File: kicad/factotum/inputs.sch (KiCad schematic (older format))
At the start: 33 parts, among them J4 Conn_01x10_Female, J5 VOCT, J6 Conn_01x10_Male, J7 SCL, J8 CLK, SW1 MODE_SW, U4 MCP6004, U5 ADC128S022

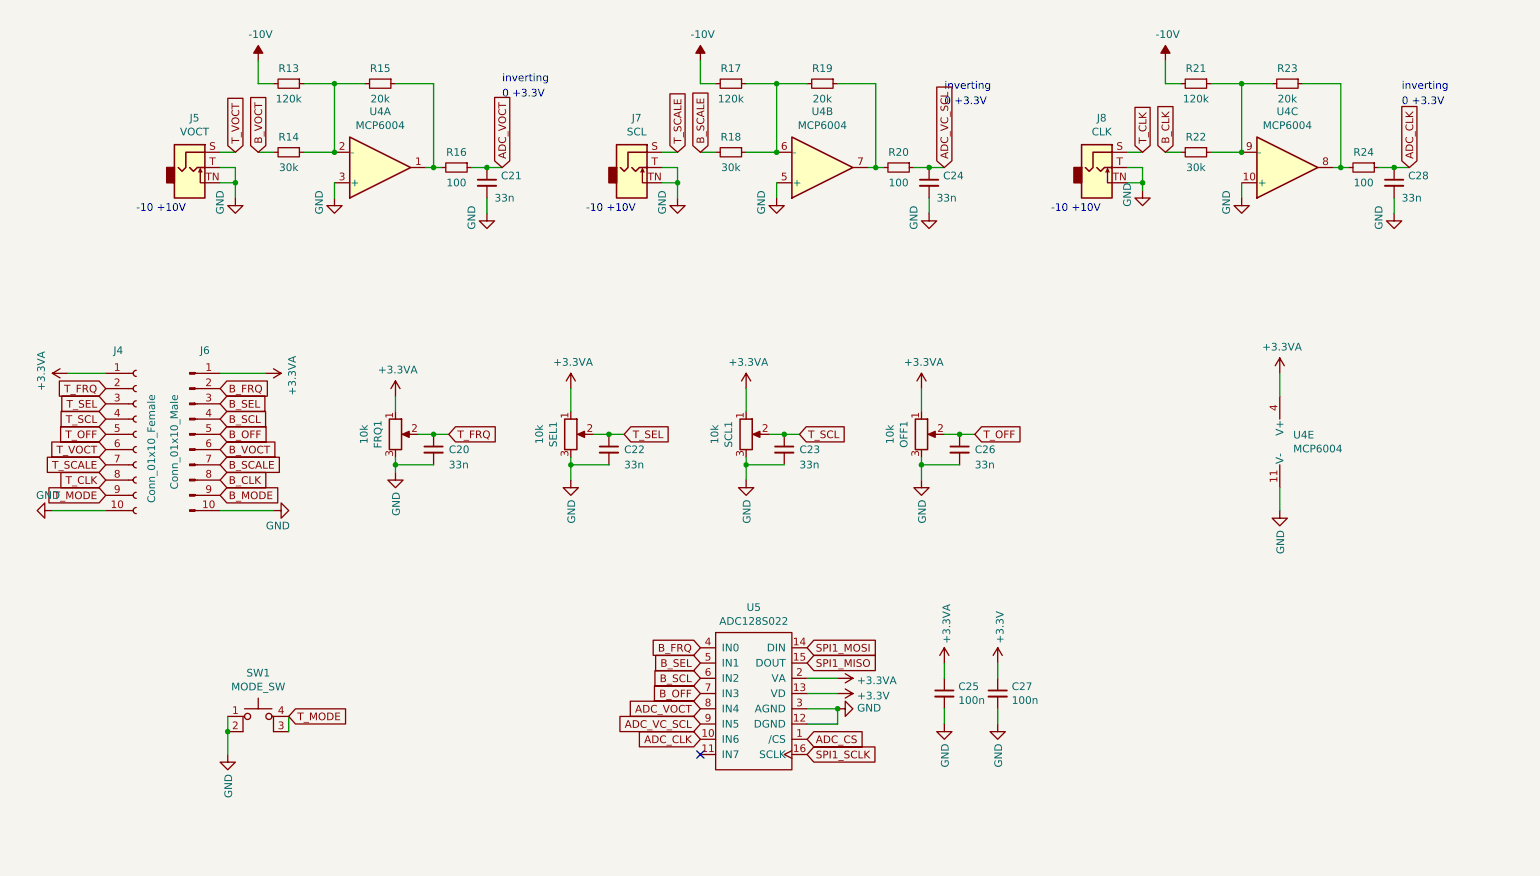
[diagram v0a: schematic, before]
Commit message: inital board layout done but not routed
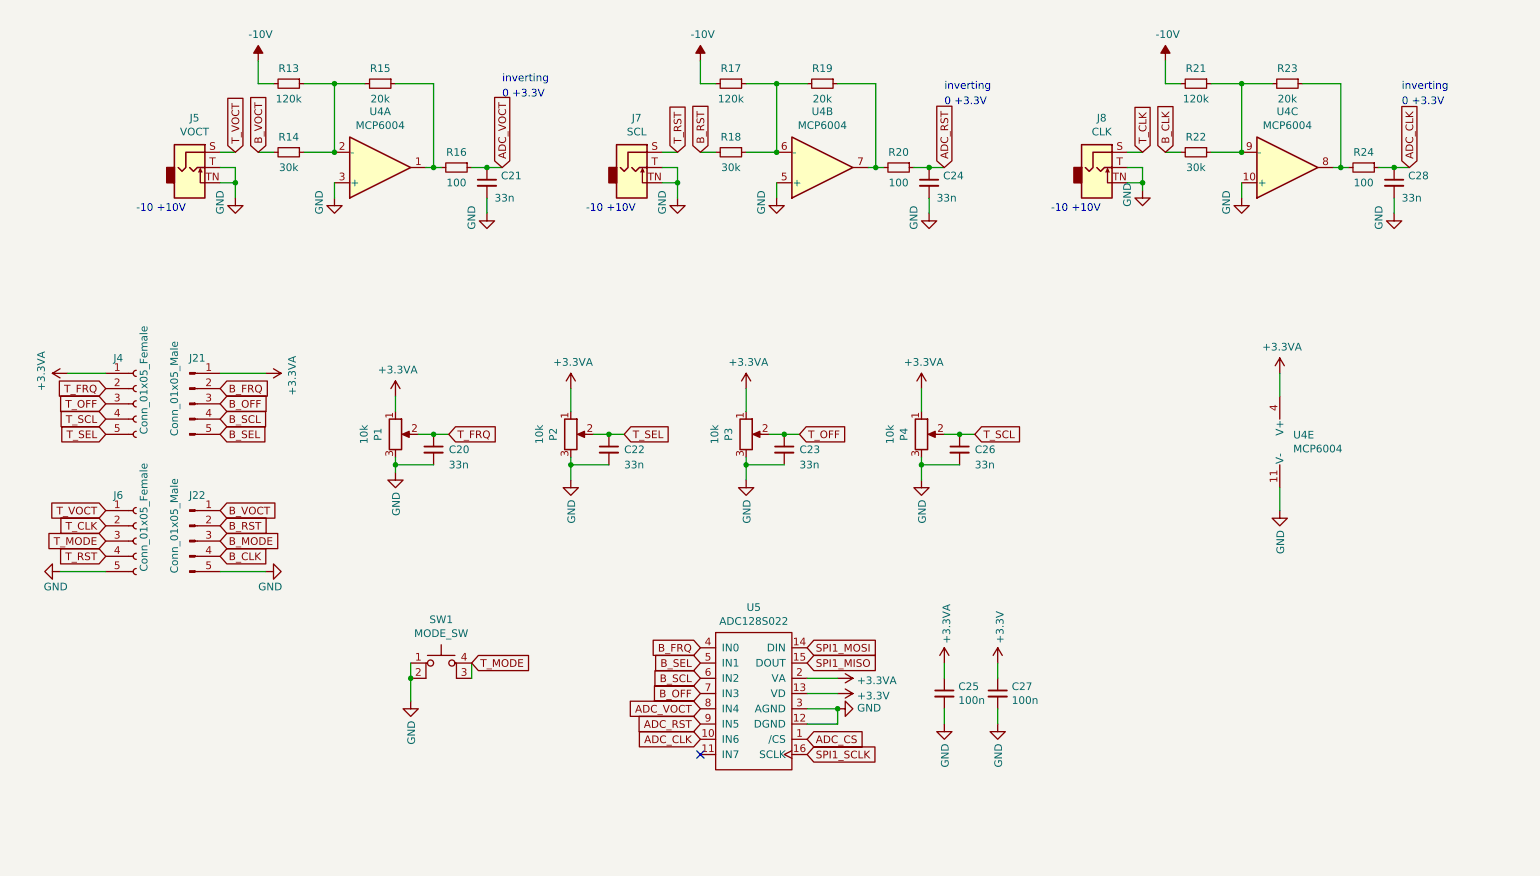
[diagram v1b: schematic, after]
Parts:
- removed J4: Conn_01x10_Female, Connector_PinSocket_1.27mm:PinSocket_1x10_P1.27mm_Vertical, symbol Connector:Conn_01x10_Female
- removed J6: Conn_01x10_Male, Connector_PinHeader_1.27mm:PinHeader_1x10_P1.27mm_Vertical, symbol Connector:Conn_01x10_Male
- added J21, J22: Conn_01x05_Male, Connector_PinHeader_2.54mm:PinHeader_1x05_P2.54mm_Vertical, symbol Connector:Conn_01x05_Male
- added J4, J6: Conn_01x05_Female, Connector_PinSocket_2.54mm:PinSocket_1x05_P2.54mm_Vertical, symbol Connector:Conn_01x05_Female
- J5: footprint (none) -> Connector_Audio:Jack_3.5mm_QingPu_WQP-PJ398SM_Vertical_CircularHoles
- renumbered FRQ1 to P1, SEL1 to P2, SCL1 to P3, OFF1 to P4
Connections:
- net +3.3VA: now also J21.1 (Pin_1), J4.1 (Pin_1)
- net B_CLK: now also J22.4 (Pin_4)
- net B_FRQ: now also J21.2 (Pin_2)
- net B_MODE: now also J22.3 (Pin_3)
- net B_OFF: now also J21.3 (Pin_3)
- net B_SCL: now also J21.4 (Pin_4)
- net B_SEL: now also J21.5 (Pin_5)
- net B_VOCT: now also J22.1 (Pin_1)
- net GND: now also J22.5 (Pin_5), J6.5 (Pin_5)
- net T_CLK: now also J6.2 (Pin_2)
- net T_FRQ: now also J4.2 (Pin_2)
- net T_MODE: now also J6.3 (Pin_3)
- net T_OFF: now also C23.1, P3.2, J4.3 (Pin_3); no longer C26.1, P4.2
- net T_SCL: now also C26.1, P4.2, J4.4 (Pin_4); no longer C23.1, P3.2
- net T_SEL: now also J4.5 (Pin_5)
- net T_VOCT: now also J6.1 (Pin_1)
- net ADC_VC_SCL renamed ADC_RST
- net B_SCALE renamed B_RST
- net B_RST: now also J22.2 (Pin_2)
- net T_SCALE renamed T_RST
- net T_RST: now also J6.4 (Pin_4)
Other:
- moved on the sheet: SW1
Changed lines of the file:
@@
 $EndComp
 Text GLabel 6600 1650 1    50   Input ~ 0
-ADC_VC_SCL
+ADC_RST
 Wire Wire Line
 	5300 1100 5500 1100
@@
 F 0 "J5" H 1682 1975 50  0000 C CNN
 F 1 "VOCT" H 1682 1884 50  0000 C CNN
-F 2 "" H 1650 1650 50  0001 C CNN
+F 2 "Connector_Audio:Jack_3.5mm_QingPu_WQP-PJ398SM_Vertical_CircularHoles" H 1650 1650 50  0001 C CNN
 F 3 "~" H 1650 1650 50  0001 C CNN
 	1    1650 1650
@@
 P 3000 3400
 AR Path="/60807EF6" Ref="FRQ?"  Part="1"
-AR Path="/606FF2F2/60807EF6" Ref="FRQ1"  Part="1"
-F 0 "FRQ1" V 2885 3400 50  0000 C CNN
+AR Path="/606FF2F2/60807EF6" Ref="P1"  Part="1"
+F 0 "P1" V 2885 3400 50  0000 C CNN
 F 1 "10k" V 2794 3400 50  0000 C CNN
 F 2 "Potentiometer_THT:Potentiometer_Alpha_RD901F-40-00D_Single_Vertical_CircularHoles" H 3000 3400 50  0001 C CNN
@@
 P 4150 3400
 AR Path="/6082088B" Ref="FRQ?"  Part="1"
-AR Path="/606FF2F2/6082088B" Ref="SEL1"  Part="1"
-F 0 "SEL1" V 4035 3400 50  0000 C CNN
+AR Path="/606FF2F2/6082088B" Ref="P2"  Part="1"
+F 0 "P2" V 4035 3400 50  0000 C CNN
 F 1 "10k" V 3944 3400 50  0000 C CNN
 F 2 "Potentiometer_THT:Potentiometer_Alpha_RD901F-40-00D_Single_Vertical_CircularHoles" H 4150 3400 50  0001 C CNN
@@
 Wire Wire Line
 	4150 3600 4150 3700
-Text GLabel 1850 3200 2    50   Input ~ 0
+Text GLabel 1850 3400 2    50   Input ~ 0
 B_SEL
 $Comp
@@
 P 5300 3400
 AR Path="/6082982D" Ref="FRQ?"  Part="1"
-AR Path="/606FF2F2/6082982D" Ref="SCL1"  Part="1"
-F 0 "SCL1" V 5185 3400 50  0000 C CNN
+AR Path="/606FF2F2/6082982D" Ref="P3"  Part="1"
+F 0 "P3" V 5185 3400 50  0000 C CNN
 F 1 "10k" V 5094 3400 50  0000 C CNN
 F 2 "Potentiometer_THT:Potentiometer_Alpha_RD901F-40-00D_Single_Vertical_CircularHoles" H 5300 3400 50  0001 C CNN
@@
 P 6450 3400
 AR Path="/60829C62" Ref="FRQ?"  Part="1"
-AR Path="/606FF2F2/60829C62" Ref="OFF1"  Part="1"
-F 0 "OFF1" V 6335 3400 50  0000 C CNN
+AR Path="/606FF2F2/60829C62" Ref="P4"  Part="1"
+F 0 "P4" V 6335 3400 50  0000 C CNN
 F 1 "10k" V 6244 3400 50  0000 C CNN
 F 2 "Potentiometer_THT:Potentiometer_Alpha_RD901F-40-00D_Single_Vertical_CircularHoles" H 6450 3400 50  0001 C CNN
@@
 Wire Wire Line
 	6450 3600 6450 3700
-Text GLabel 1850 3400 2    50   Input ~ 0
+Text GLabel 1850 3200 2    50   Input ~ 0
 B_OFF
 Text GLabel 5000 4800 0    50   Input ~ 0
@@
 ADC_VOCT
 Text GLabel 5000 5300 0    50   Input ~ 0
-ADC_VC_SCL
+ADC_RST
 Text GLabel 5000 5400 0    50   Input ~ 0
 ADC_CLK
@@
 L Switch:SW_MEC_5E SW1
 U 1 1 60C7CA31
-P 2100 5350
-F 0 "SW1" H 2100 5735 50  0000 C CNN
-F 1 "MODE_SW" H 2100 5644 50  0000 C CNN
-F 2 "Button_Switch_THT:SW_TH_Tactile_Omron_B3F-10xx" H 2100 5650 50  0001 C CNN
-F 3 "http://www.apem.com/int/index.php?controller=attachment&id_attachment=1371" H 2100 5650 50  0001 C CNN
-	1    2100 5350
+P 3300 5000
+F 0 "SW1" H 3300 5385 50  0000 C CNN
+F 1 "MODE_SW" H 3300 5294 50  0000 C CNN
+F 2 "Button_Switch_THT:SW_TH_Tactile_Omron_B3F-10xx" H 3300 5300 50  0001 C CNN
+F 3 "http://www.apem.com/int/index.php?controller=attachment&id_attachment=1371" H 3300 5300 50  0001 C CNN
+	1    3300 5000
 	1    0    0    -1
 $EndComp
@@
 L power:GND #PWR?
 U 1 1 60C7DEEC
-P 1900 5500
+P 3100 5150
 AR Path="/60C7DEEC" Ref="#PWR?"  Part="1"
 AR Path="/606FF2F2/60C7DEEC" Ref="#PWR031"  Part="1"
-F 0 "#PWR031" H 1900 5250 50  0001 C CNN
-F 1 "GND" V 1905 5372 50  0000 R CNN
-F 2 "" H 1900 5500 50  0001 C CNN
-F 3 "" H 1900 5500 50  0001 C CNN
-	1    1900 5500
-	1    0    0    -1
-$EndComp
-Wire Wire Line
-	1900 5500 1900 5350
-Connection ~ 1900 5350
-Wire Wire Line
-	1900 5350 1900 5250
-Text GLabel 2300 5250 2    50   Input ~ 0
+F 0 "#PWR031" H 3100 4900 50  0001 C CNN
+F 1 "GND" V 3105 5022 50  0000 R CNN
+F 2 "" H 3100 5150 50  0001 C CNN
+F 3 "" H 3100 5150 50  0001 C CNN
+	1    3100 5150
+	1    0    0    -1
+$EndComp
+Wire Wire Line
+	3100 5150 3100 5000
+Connection ~ 3100 5000
+Wire Wire Line
+	3100 5000 3100 4900
+Text GLabel 3500 4900 2    50   Input ~ 0
 T_MODE
 Wire Wire Line
-	2300 5250 2300 5350
-$Comp
-L Connector:Conn_01x10_Female J4
-U 1 1 5FC3B5C0
-P 1300 3400
-F 0 "J4" H 1150 3950 50  0000 L CNN
-F 1 "Conn_01x10_Female" V 1400 2950 50  0000 L CNN
-F 2 "Connector_PinSocket_1.27mm:PinSocket_1x10_P1.27mm_Vertical" H 1300 3400 50  0001 C CNN
-F 3 "~" H 1300 3400 50  0001 C CNN
-	1    1300 3400
-	1    0    0    -1
-$EndComp
-$Comp
-L Connector:Conn_01x10_Male J6
-U 1 1 5FC3DD64
-P 1650 3400
-F 0 "J6" H 1750 3950 50  0000 C CNN
-F 1 "Conn_01x10_Male" V 1550 3350 50  0000 C CNN
-F 2 "Connector_PinHeader_1.27mm:PinHeader_1x10_P1.27mm_Vertical" H 1650 3400 50  0001 C CNN
-F 3 "~" H 1650 3400 50  0001 C CNN
-	1    1650 3400
-	1    0    0    -1
-$EndComp
+	3500 4900 3500 5000
 Wire Wire Line
 	3000 3550 3000 3600
@@
 Text GLabel 4500 3400 2    50   Input ~ 0
 T_SEL
-Text GLabel 1100 3200 0    50   Input ~ 0
+Text GLabel 1100 3400 0    50   Input ~ 0
 T_SEL
 Connection ~ 5550 3400
@@
 Wire Wire Line
 	6700 3600 6450 3600
+Text GLabel 6800 3400 2    50   Input ~ 0
+T_SCL
 Text GLabel 5650 3400 2    50   Input ~ 0
-T_SCL
-Text GLabel 6800 3400 2    50   Input ~ 0
 T_OFF
-Text GLabel 1100 3400 0    50   Input ~ 0
+Text GLabel 1100 3200 0    50   Input ~ 0
 T_OFF
 Text GLabel 1100 3300 0    50   Input ~ 0
@@
 Text GLabel 1950 1550 1    50   Input ~ 0
 T_VOCT
-Text GLabel 1100 3500 0    50   Input ~ 0
+Text GLabel 1100 3900 0    50   Input ~ 0
 T_VOCT
 Text GLabel 2100 1550 1    50   Input ~ 0
 B_VOCT
-Text GLabel 1850 3500 2    50   Input ~ 0
+Text GLabel 1850 3900 2    50   Input ~ 0
 B_VOCT
 Text GLabel 4850 1550 1    50   Input ~ 0
-T_SCALE
+T_RST
 Wire Wire Line
 	8350 1550 8550 1550
 Connection ~ 8550 1550
 Text GLabel 5000 1550 1    50   Input ~ 0
-B_SCALE
+B_RST
 Text GLabel 7900 1550 1    50   Input ~ 0
 T_CLK
 Text GLabel 8050 1550 1    50   Input ~ 0
 B_CLK
-Text GLabel 1100 3600 0    50   Input ~ 0
-T_SCALE
-Text GLabel 1850 3600 2    50   Input ~ 0
-B_SCALE
-Text GLabel 1100 3700 0    50   Input ~ 0
+Text GLabel 1100 4200 0    50   Input ~ 0
+T_RST
+Text GLabel 1850 4000 2    50   Input ~ 0
+B_RST
+Text GLabel 1100 4000 0    50   Input ~ 0
 T_CLK
-Text GLabel 1850 3700 2    50   Input ~ 0
+Text GLabel 1850 4200 2    50   Input ~ 0
 B_CLK
-Text GLabel 1850 3800 2    50   Input ~ 0
+Text GLabel 1850 4100 2    50   Input ~ 0
 B_MODE
-Text GLabel 1100 3800 0    50   Input ~ 0
+Text GLabel 1100 4100 0    50   Input ~ 0
 T_MODE
 $Comp
@@
 L power:GND #PWR?
 U 1 1 5FE18FBB
-P 750 3900
+P 800 4300
 AR Path="/5FE18FBB" Ref="#PWR?"  Part="1"
 AR Path="/606FF2F2/5FE18FBB" Ref="#PWR029"  Part="1"
-F 0 "#PWR029" H 750 3650 50  0001 C CNN
-F 1 "GND" V 650 3950 50  0000 R CNN
-F 2 "" H 750 3900 50  0001 C CNN
-F 3 "" H 750 3900 50  0001 C CNN
-	1    750  3900
+F 0 "#PWR029" H 800 4050 50  0001 C CNN
+F 1 "GND" V 900 4350 50  0000 R CNN
+F 2 "" H 800 4300 50  0001 C CNN
+F 3 "" H 800 4300 50  0001 C CNN
+	1    800  4300
 	0    1    1    0
 $EndComp
@@
 L power:GND #PWR?
 U 1 1 5FE1CBFF
-P 2200 3900
+P 2150 4300
 AR Path="/5FE1CBFF" Ref="#PWR?"  Part="1"
 AR Path="/606FF2F2/5FE1CBFF" Ref="#PWR035"  Part="1"
-F 0 "#PWR035" H 2200 3650 50  0001 C CNN
-F 1 "GND" V 2100 3950 50  0000 R CNN
-F 2 "" H 2200 3900 50  0001 C CNN
-F 3 "" H 2200 3900 50  0001 C CNN
-	1    2200 3900
+F 0 "#PWR035" H 2150 4050 50  0001 C CNN
+F 1 "GND" V 2050 4350 50  0000 R CNN
+F 2 "" H 2150 4300 50  0001 C CNN
+F 3 "" H 2150 4300 50  0001 C CNN
+	1    2150 4300
 	0    -1   -1   0
 $EndComp
@@
 Wire Wire Line
 	1850 3000 2150 3000
-Wire Wire Line
-	750  3900 1100 3900
-Wire Wire Line
-	1850 3900 2200 3900
 Wire Wire Line
 	1850 1650 1950 1650
@@
 Wire Wire Line
 	9550 1850 9550 1950
+$Comp
+L Connector:Conn_01x05_Female J4
+U 1 1 5FD0067F
+P 1300 3200
+F 0 "J4" H 1150 3500 50  0000 L CNN
+F 1 "Conn_01x05_Female" V 1350 3000 50  0000 L CNN
+F 2 "Connector_PinSocket_2.54mm:PinSocket_1x05_P2.54mm_Vertical" H 1300 3200 50  0001 C CNN
+F 3 "~" H 1300 3200 50  0001 C CNN
+	1    1300 3200
+	1    0    0    -1
+$EndComp
+$Comp
+L Connector:Conn_01x05_Male J21
+U 1 1 5FD01CE2
+P 1650 3200
+F 0 "J21" H 1700 3500 50  0000 C CNN
+F 1 "Conn_01x05_Male" V 1550 3300 50  0000 C CNN
+F 2 "Connector_PinHeader_2.54mm:PinHeader_1x05_P2.54mm_Vertical" H 1650 3200 50  0001 C CNN
+F 3 "~" H 1650 3200 50  0001 C CNN
+	1    1650 3200
+	1    0    0    -1
+$EndComp
+$Comp
+L Connector:Conn_01x05_Female J6
+U 1 1 5FD0B497
+P 1300 4100
+F 0 "J6" H 1150 4400 50  0000 L CNN
+F 1 "Conn_01x05_Female" V 1350 3900 50  0000 L CNN
+F 2 "Connector_PinSocket_2.54mm:PinSocket_1x05_P2.54mm_Vertical" H 1300 4100 50  0001 C CNN
+F 3 "~" H 1300 4100 50  0001 C CNN
+	1    1300 4100
+	1    0    0    -1
+$EndComp
+$Comp
+L Connector:Conn_01x05_Male J22
+U 1 1 5FD0B85D
+P 1650 4100
+F 0 "J22" H 1700 4400 50  0000 C CNN
+F 1 "Conn_01x05_Male" V 1550 4200 50  0000 C CNN
+F 2 "Connector_PinHeader_2.54mm:PinHeader_1x05_P2.54mm_Vertical" H 1650 4100 50  0001 C CNN
+F 3 "~" H 1650 4100 50  0001 C CNN
+	1    1650 4100
+	1    0    0    -1
+$EndComp
+Wire Wire Line
+	2150 4300 1850 4300
+Wire Wire Line
+	1100 4300 800  4300
 $EndSCHEMATC

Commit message: adding switches to inputs; fixing resistor components to 603
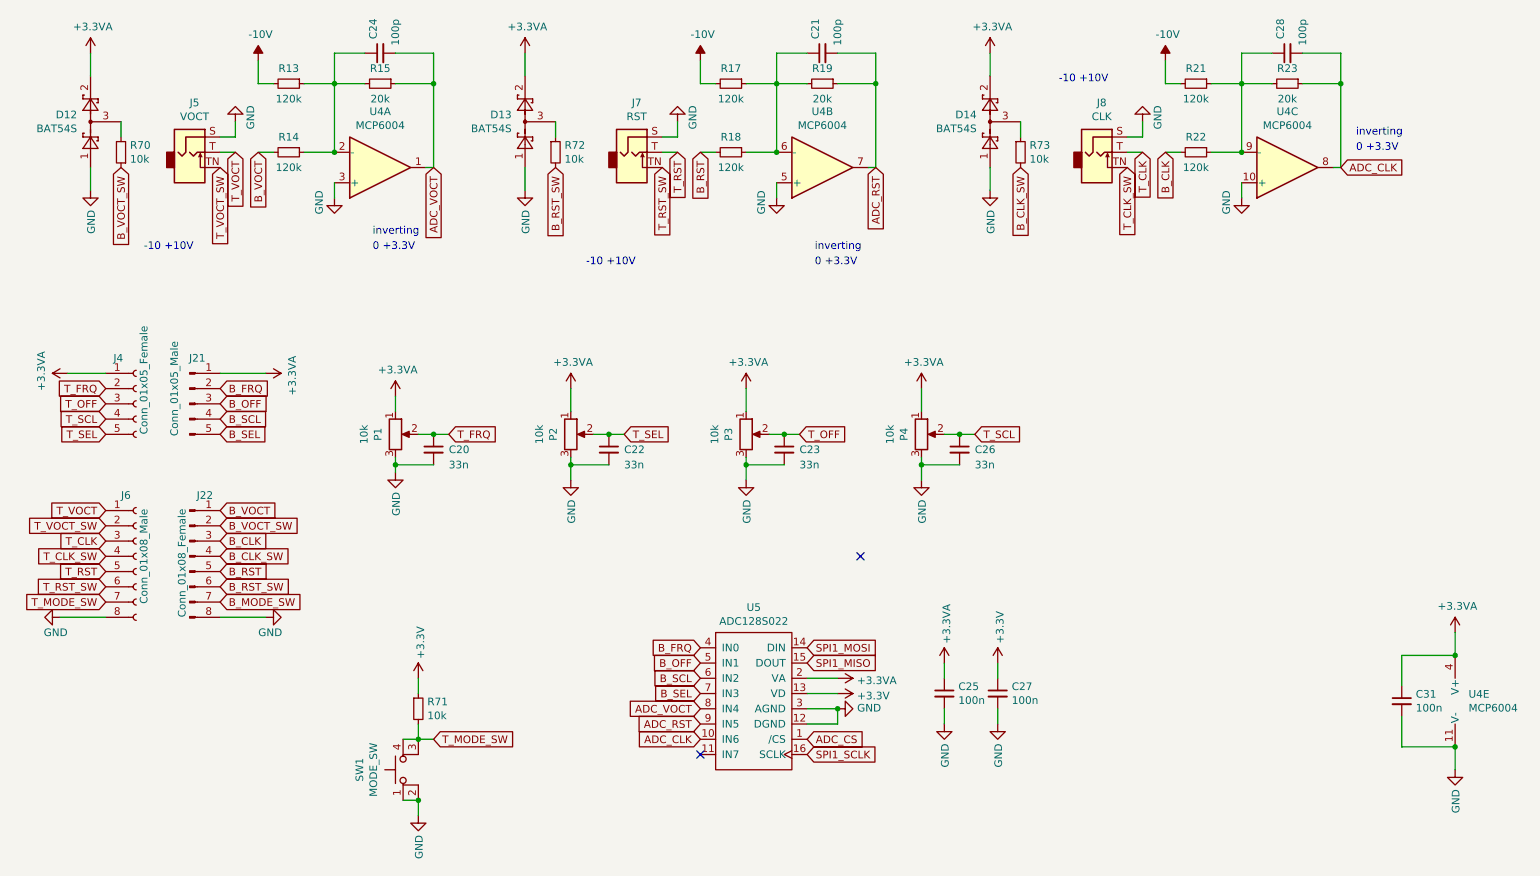
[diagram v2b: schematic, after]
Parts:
- removed J22: Conn_01x05_Male, Connector_PinHeader_2.54mm:PinHeader_1x05_P2.54mm_Vertical, symbol Connector:Conn_01x05_Male
- removed J6: Conn_01x05_Female, Connector_PinSocket_2.54mm:PinSocket_1x05_P2.54mm_Vertical, symbol Connector:Conn_01x05_Female
- removed R16, R20, R24: 100, Resistor_SMD:R_0201_0603Metric_Pad0.64x0.40mm_HandSolder, symbol Device:R_Small
- added C31: 100n, Capacitor_SMD:C_0603_1608Metric_Pad1.08x0.95mm_HandSolder, symbol Device:C_Small
- added D12, D13, D14: BAT54S, Package_TO_SOT_SMD:SOT-23, symbol Diode:BAT54S
- added J22: Conn_01x08_Male, Connector_PinHeader_2.54mm:PinHeader_1x08_P2.54mm_Vertical, symbol Connector:Conn_01x08_Male
- added J6: Conn_01x08_Female, Connector_PinSocket_2.54mm:PinSocket_1x08_P2.54mm_Vertical, symbol Connector:Conn_01x08_Female
- added R70, R71, R72, R73: 10k, Resistor_SMD:R_0603_1608Metric_Pad0.98x0.95mm_HandSolder, symbol Device:R_Small
- C21, C24, C28: value 33n -> 100p
- J7: value SCL -> RST
- R13, R15, R17, R19, R21, R23: footprint Resistor_SMD:R_0201_0603Metric_Pad0.64x0.40mm_HandSolder -> Resistor_SMD:R_0603_1608Metric_Pad0.98x0.95mm_HandSolder
- R14, R18, R22: value 30k -> 120k; footprint Resistor_SMD:R_0201_0603Metric_Pad0.64x0.40mm_HandSolder -> Resistor_SMD:R_0603_1608Metric_Pad0.98x0.95mm_HandSolder
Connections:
- net +3.3VA: now also C31.1, D12.2, D13.2, D14.2
- net +3V3: now also R71.1
- net ADC_CLK: now also C28.2, R23.1, U4.8; no longer C28.1
- net ADC_RST: now also C21.2, R19.1, U4.7; no longer C24.1
- net ADC_VOCT: now also C24.2, R15.1, U4.1; no longer C21.1
- net B_CLK: now also J22.3 (Pin_3)
- net B_OFF: now also U5.5 (IN1); no longer U5.7 (IN3)
- net B_RST: now also J22.5 (Pin_5)
- net B_SEL: now also U5.7 (IN3); no longer U5.5 (IN1)
- net B_VOCT: now also J22.1 (Pin_1)
- net GND: now also J5.S, J7.S, J8.S, C31.2, D12.1, D13.1, D14.1, J22.8 (Pin_8), J6.8 (Pin_8); no longer C21.2, C24.2, C28.2, J5.T, J5.TN, J7.T, J7.TN, J8.T, J8.TN
- net T_CLK: now also J8.T, J6.3 (Pin_3); no longer J8.S
- net T_RST: now also J7.T, J6.5 (Pin_5); no longer J7.S
- net T_VOCT: now also J5.T, J6.1 (Pin_1); no longer J5.S
- net at R17.1, R18.1, R19.2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: now also C21.1
- net at R21.1, R22.1, R23.2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: now also C28.1
- net at R13.1, R14.1, R15.2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: now also C24.1
- net T_MODE renamed T_MODE_SW
- net T_MODE_SW: now also J6.7 (Pin_7), R71.2
- new net: D12.3, R70.2
- new net: D13.3, R72.1
- new net: D14.3, R73.1
- new net B_CLK_SW: J22.4 (Pin_4), R73.2
- new net B_MODE_SW: J22.7 (Pin_7)
- new net B_RST_SW: J22.6 (Pin_6), R72.2
- new net B_VOCT_SW: J22.2 (Pin_2), R70.1
- new net T_CLK_SW: J6.4 (Pin_4), J8.TN
- new net T_RST_SW: J6.6 (Pin_6), J7.TN
- new net T_VOCT_SW: J5.TN, J6.2 (Pin_2)
- no-connect marks 1 -> 2
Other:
- moved on the sheet: C24, J5, J7, J8, SW1, U4E
